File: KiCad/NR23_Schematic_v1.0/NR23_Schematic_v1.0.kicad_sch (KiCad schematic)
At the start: 0 parts

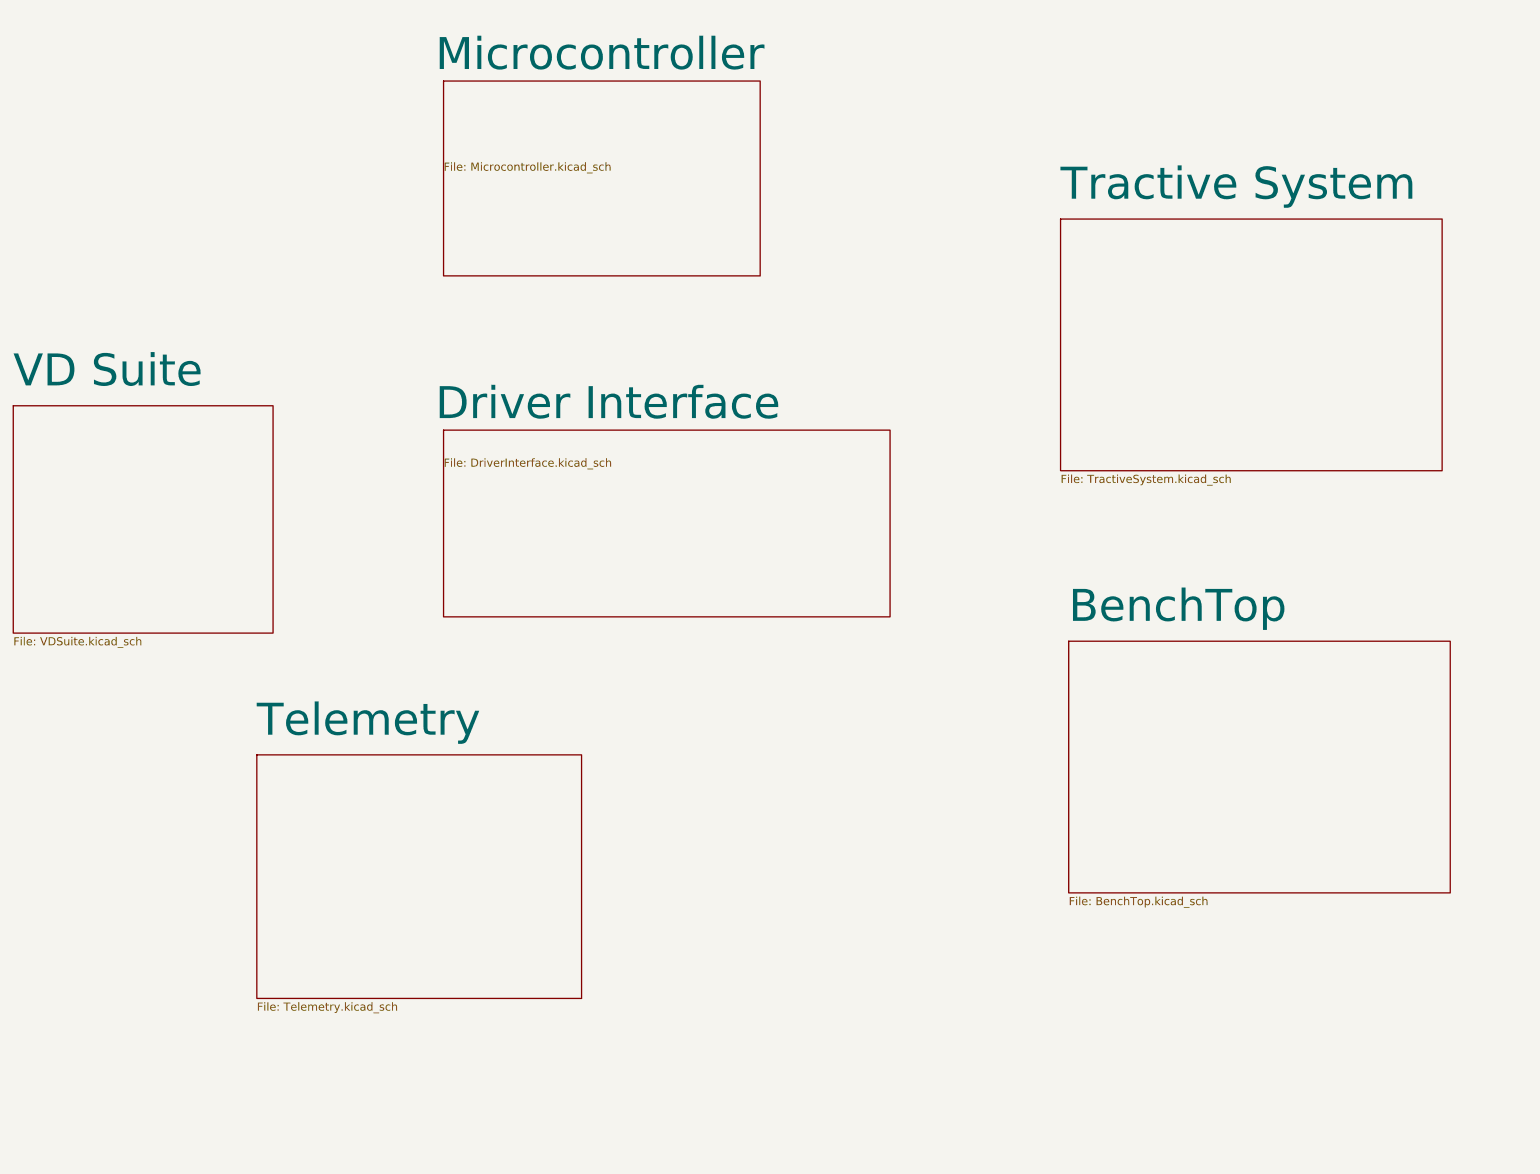
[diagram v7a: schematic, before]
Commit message: added TI board box on the Tractive System Schematc
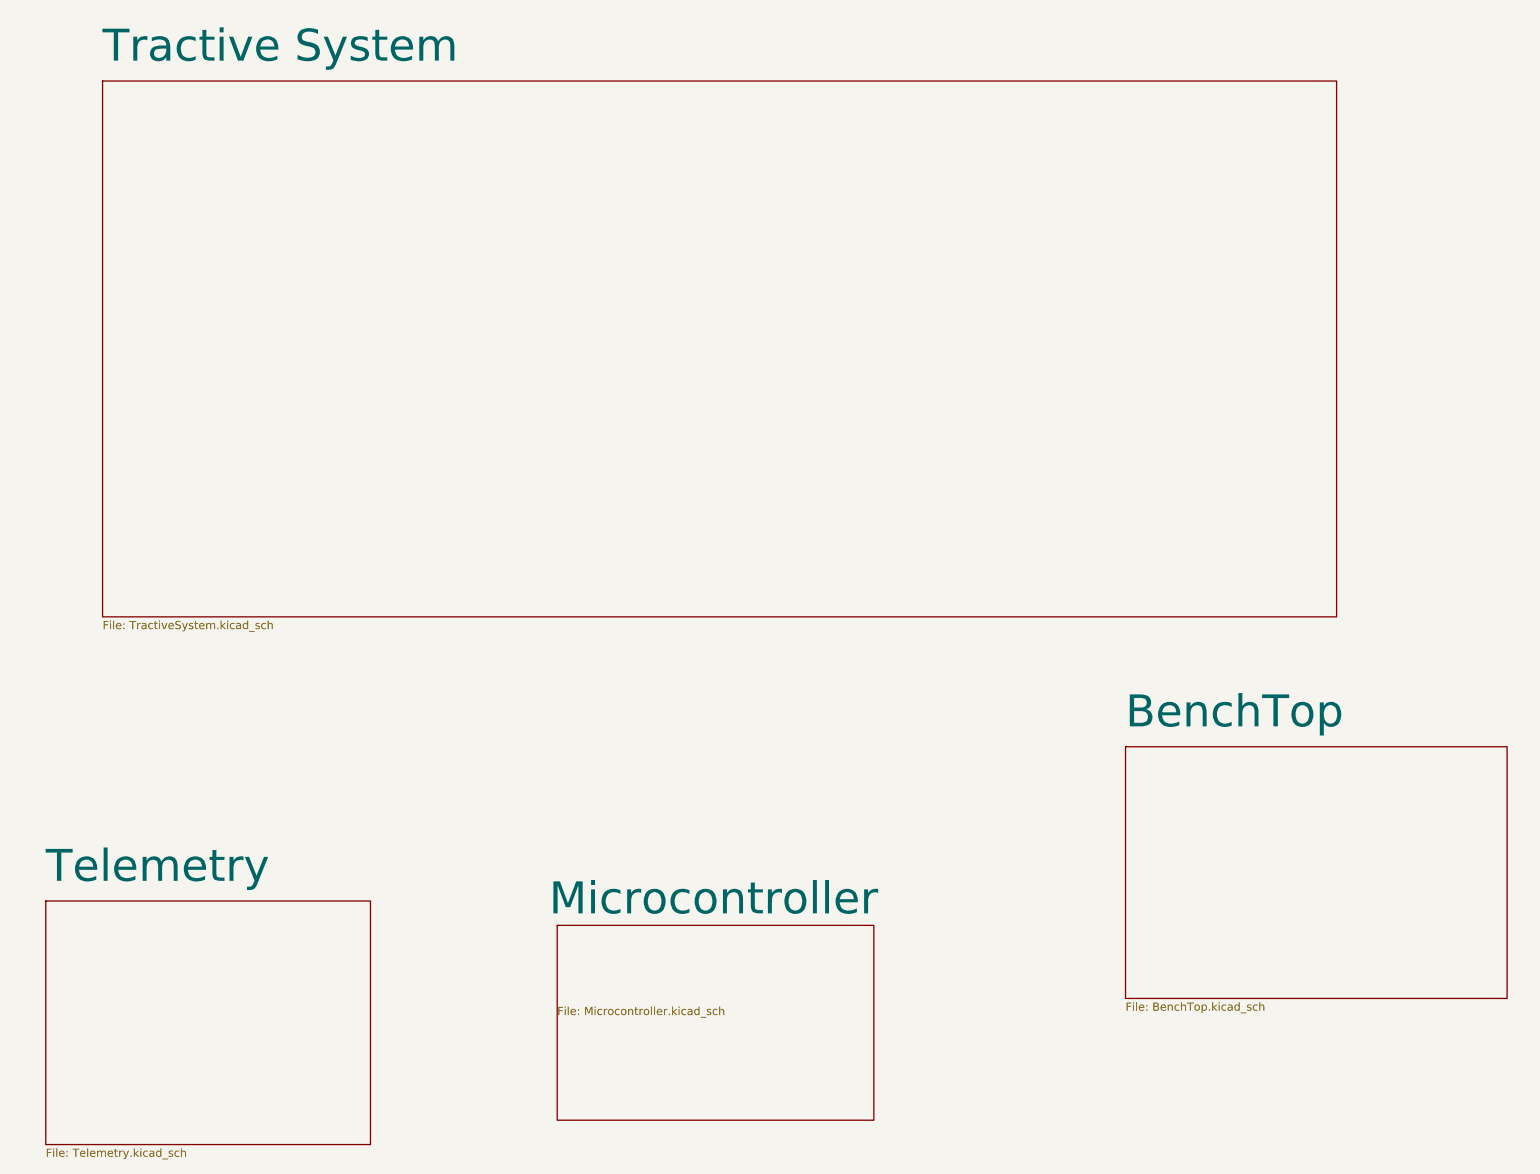
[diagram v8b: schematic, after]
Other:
- removed sheet Driver Interface
- removed sheet VD Suite
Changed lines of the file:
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@@
   (paper "A")
   (title_block
-    (date "2023-03-03")
+    (date "2023-04-04")
   )
-  (sheet (at 59.69 133.35) (size 50.8 38.1)
+  (sheet (at 26.67 156.21) (size 50.8 38.1)
     (stroke (width 0.1524) (type solid) (color 0 0 0 0))
     (fill (color 0 0 0 0.0000))
-    (property "Sheet name" "Telemetry" (id 0) (at 59.69 130.81 0)
+    (property "Sheet name" "Telemetry" (id 0) (at 26.67 153.67 0)
       (effects (font (size 5 5)) (justify left bottom))
     )
-    (property "Sheet file" "Telemetry.kicad_sch" (id 1) (at 59.69 172.0346 0)
+    (property "Sheet file" "Telemetry.kicad_sch" (id 1) (at 26.67 194.8946 0)
       (effects (font (size 1.27 1.27)) (justify left top))
     )
   )
-  (sheet (at 21.59 78.74) (size 40.64 35.56) (fields_autoplaced)
+  (sheet (at 195.58 132.08) (size 59.69 39.37) (fields_autoplaced)
     (stroke (width 0.1524) (type solid) (color 0 0 0 0))
     (fill (color 0 0 0 0.0000))
-    (property "Sheet name" "VD Suite" (id 0) (at 21.59 76.1634 0)
+    (property "Sheet name" "BenchTop" (id 0) (at 195.58 129.5034 0)
       (effects (font (size 5 5)) (justify left bottom))
     )
-    (property "Sheet file" "VDSuite.kicad_sch" (id 1) (at 21.59 114.8846 0)
+    (property "Sheet file" "BenchTop.kicad_sch" (id 1) (at 195.58 172.0346 0)
       (effects (font (size 1.27 1.27)) (justify left top))
     )
   )
-  (sheet (at 88.9 82.55) (size 69.85 29.21)
+  (sheet (at 35.56 27.94) (size 193.04 83.82) (fields_autoplaced)
     (stroke (width 0.1524) (type solid) (color 0 0 0 0))
     (fill (color 0 0 0 0.0000))
-    (property "Sheet name" "Driver Interface" (id 0) (at 87.63 81.28 0)
+    (property "Sheet name" "Tractive System" (id 0) (at 35.56 25.3634 0)
       (effects (font (size 5 5)) (justify left bottom))
     )
-    (property "Sheet file" "DriverInterface.kicad_sch" (id 1) (at 88.9 86.9446 0)
+    (property "Sheet file" "TractiveSystem.kicad_sch" (id 1) (at 35.56 112.3446 0)
       (effects (font (size 1.27 1.27)) (justify left top))
     )
   )
-  (sheet (at 186.69 115.57) (size 59.69 39.37) (fields_autoplaced)
+  (sheet (at 106.68 160.02) (size 49.53 30.48)
     (stroke (width 0.1524) (type solid) (color 0 0 0 0))
     (fill (color 0 0 0 0.0000))
-    (property "Sheet name" "BenchTop" (id 0) (at 186.69 112.9934 0)
+    (property "Sheet name" "Microcontroller" (id 0) (at 105.41 158.75 0)
       (effects (font (size 5 5)) (justify left bottom))
     )
-    (property "Sheet file" "BenchTop.kicad_sch" (id 1) (at 186.69 155.5246 0)
-      (effects (font (size 1.27 1.27)) (justify left top))
-    )
-  )
-  (sheet (at 185.42 49.53) (size 59.69 39.37) (fields_autoplaced)
-    (stroke (width 0.1524) (type solid) (color 0 0 0 0))
-    (fill (color 0 0 0 0.0000))
-    (property "Sheet name" "Tractive System" (id 0) (at 185.42 46.9534 0)
-      (effects (font (size 5 5)) (justify left bottom))
-    )
-    (property "Sheet file" "TractiveSystem.kicad_sch" (id 1) (at 185.42 89.4846 0)
-      (effects (font (size 1.27 1.27)) (justify left top))
-    )
-  )
-  (sheet (at 88.9 27.94) (size 49.53 30.48)
-    (stroke (width 0.1524) (type solid) (color 0 0 0 0))
-    (fill (color 0 0 0 0.0000))
-    (property "Sheet name" "Microcontroller" (id 0) (at 87.63 26.67 0)
-      (effects (font (size 5 5)) (justify left bottom))
-    )
-    (property "Sheet file" "Microcontroller.kicad_sch" (id 1) (at 88.9 40.64 0)
+    (property "Sheet file" "Microcontroller.kicad_sch" (id 1) (at 106.68 172.72 0)
       (effects (font (size 1.27 1.27)) (justify left top))
     )
@@
   (sheet_instances
     (path "/" (page "1"))
+    (path "/8302703f-65d0-4b91-aeea-6f721ab57e4c" (page "1"))
     (path "/c7466bb0-ebde-4ea4-90e3-94511e3895a3" (page "2"))
-    (path "/40c358ae-a01e-49c6-aef1-9b414ada72a7" (page "3"))
-    (path "/2df3fecd-d45b-4e25-bac9-628d20876953" (page "4"))
     (path "/16ced548-a4c4-4a05-b722-8e9610f878cc" (page "5"))
-    (path "/8302703f-65d0-4b91-aeea-6f721ab57e4c" (page "6"))
     (path "/6b38ef1b-89ba-46d1-8032-b895c26a5218" (page "7"))
   )
@@
       (reference "SW?") (unit 1) (value "Shifter Switch") (footprint "")
     )
+    (path "/6b38ef1b-89ba-46d1-8032-b895c26a5218/839a2160-4be7-4a71-b4f3-e2d027441525"
+      (reference "SW?") (unit 1) (value "HV Safety Switch") (footprint "")
+    )
     (path "/8302703f-65d0-4b91-aeea-6f721ab57e4c/839a2160-4be7-4a71-b4f3-e2d027441525"
       (reference "SW?") (unit 1) (value "HV Safety Switch (behind driver)") (footprint "")
-    )
-    (path "/6b38ef1b-89ba-46d1-8032-b895c26a5218/839a2160-4be7-4a71-b4f3-e2d027441525"
-      (reference "SW?") (unit 1) (value "HV Safety Switch") (footprint "")
     )
     (path "/8302703f-65d0-4b91-aeea-6f721ab57e4c/ab1e632e-d4c8-4dc8-b13f-a9f28de904e4"
@@
       (reference "SW?") (unit 1) (value "100V E-stop (Right)") (footprint "")
     )
-    (path "/6b38ef1b-89ba-46d1-8032-b895c26a5218/0aa54167-f3d9-467b-bc69-db1827651c6c"
+    (path "/8302703f-65d0-4b91-aeea-6f721ab57e4c/0aa54167-f3d9-467b-bc69-db1827651c6c"
       (reference "U?") (unit 1) (value "Throttle") (footprint "")
     )
-    (path "/8302703f-65d0-4b91-aeea-6f721ab57e4c/0aa54167-f3d9-467b-bc69-db1827651c6c"
+    (path "/6b38ef1b-89ba-46d1-8032-b895c26a5218/0aa54167-f3d9-467b-bc69-db1827651c6c"
       (reference "U?") (unit 1) (value "Throttle") (footprint "")
     )
@@
       (reference "U?") (unit 1) (value "TI_J12_CANbus") (footprint "")
     )
-    (path "/40c358ae-a01e-49c6-aef1-9b414ada72a7/86cf8333-4281-49ef-8de9-d09a4c2f7e61"
-      (reference "U?") (unit 1) (value "Dash") (footprint "")
-    )
     (path "/16ced548-a4c4-4a05-b722-8e9610f878cc/942b0a04-1bf0-4324-8c6e-417346d8e5d0"
